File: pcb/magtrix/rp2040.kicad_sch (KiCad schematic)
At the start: 31 parts, among them J1 Conn_01x08_Pin, SW1 SW_MEC_5E, SW2 SW_MEC_5E, U1 W25Q128JVS, U3 RP2040, U4 AMS1117-3.3, Y1 12Mhz

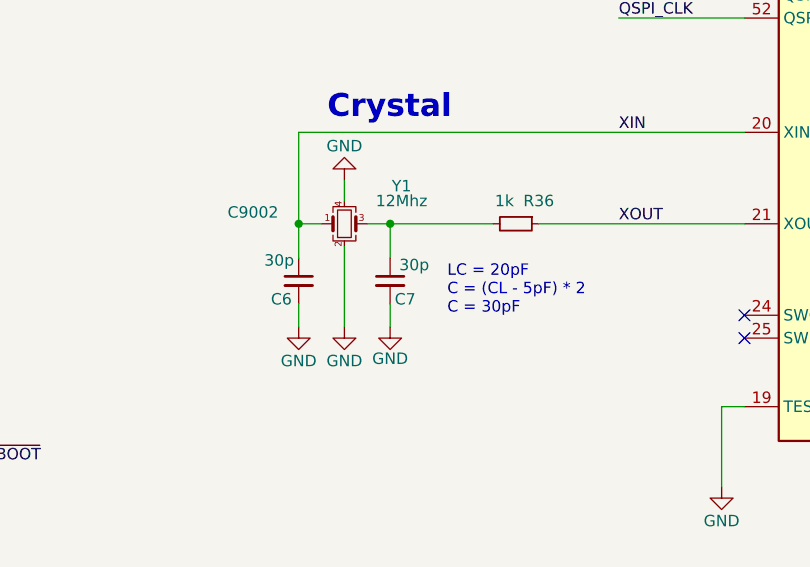
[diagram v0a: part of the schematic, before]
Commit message: Finished schematics and footprints, need to redo the placement
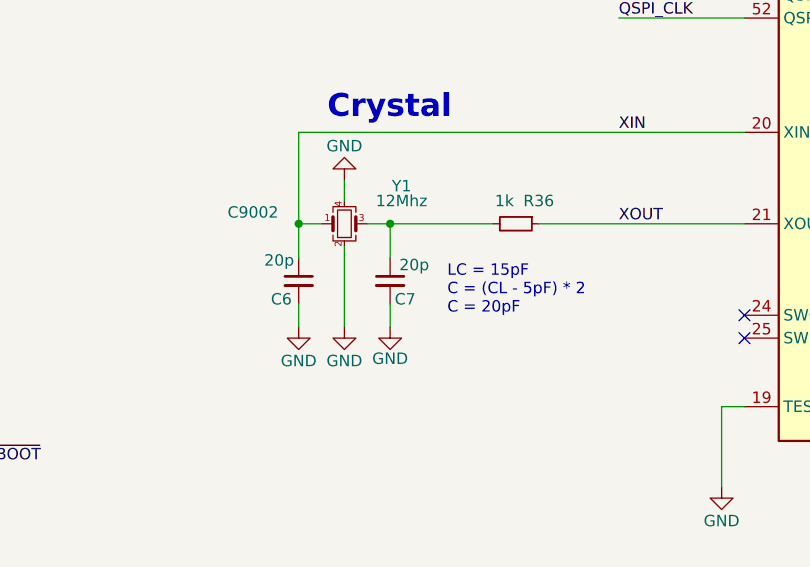
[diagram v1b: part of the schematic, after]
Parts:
- C10, C11: MFR (none) -> CL10A105KA8NNNC; MOUSER (none) -> 187-CL10A105KA8NNNC
- C12, C13, C14, C15, C16, C17, C3, C8, C9: MFR (none) -> TMK107BJ104KA-T; MOUSER (none) -> 963-TMK107BJ104KA-T
- C18, C19: footprint Capacitor_SMD:C_0603_1608Metric_Pad1.08x0.95mm_HandSolder -> Capacitor_SMD:C_1206_3216Metric; MFR (none) -> CL31A106MBHNNNE; MOUSER (none) -> 187-CL31A106MBHNNNE
- C6, C7: value 30p -> 20p; MFR (none) -> CL10C200JB8NNNC; MOUSER (none) -> 187-CL10C200JB8NNNC
- J1: footprint (none) -> Connector_PinHeader_1.00mm:PinHeader_1x08_P1.00mm_Vertical_SMD_Pin1Left
- R33, R35: MFR (none) -> CRCW060310K0JNEC; MOUSER (none) -> 71-CRCW060310K0JNEC
- R34, R36: footprint Resistor_SMD:R_0603_1608Metric -> Resistor_SMD:R_1206_3216Metric; MFR (none) -> ERJ-S08F1001V; MOUSER (none) -> 667-ERJ-S08F1001V
- R37, R38: MFR (none) -> CRCW060333R0JNEA; MOUSER (none) -> 71-CRCW0603J-33-E3
- R39, R40: MFR (none) -> CR0603AFX-5101EAS; MOUSER (none) -> 652-CR0603AFX5101EAS
- U1: MFR (none) -> W25Q128JVSIM; MOUSER (none) -> 454-W25Q128JVSIM
- U3: MFR (none) -> SC0914(13); MOUSER (none) -> 358-SC091413
- U4: MFR (none) -> LM1117MPX-3.3/NOPB; MOUSER (none) -> 926-LM1117MPX3.3NOPB
- Y1: footprint Crystal:Crystal_SMD_3225-4Pin_3.2x2.5mm -> CRYSTAL:crystal; MFR (none) -> 830069944; MOUSER (none) -> 710-830069944
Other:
- note added: "LC = 15pF C = (CL - 5pF) * 2 C = 20pF"
- note removed: "LC = 20pF C = (CL - 5pF) * 2 C = 30pF"

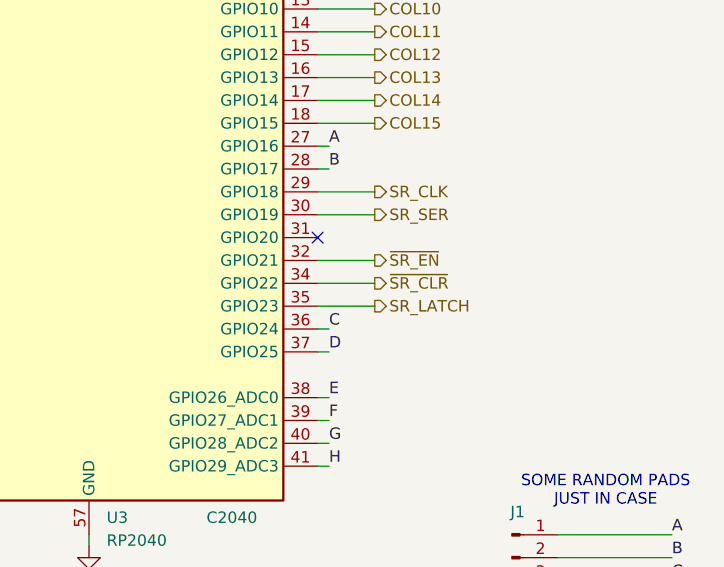
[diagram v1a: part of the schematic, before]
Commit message: Changed shift registers to open drain ones
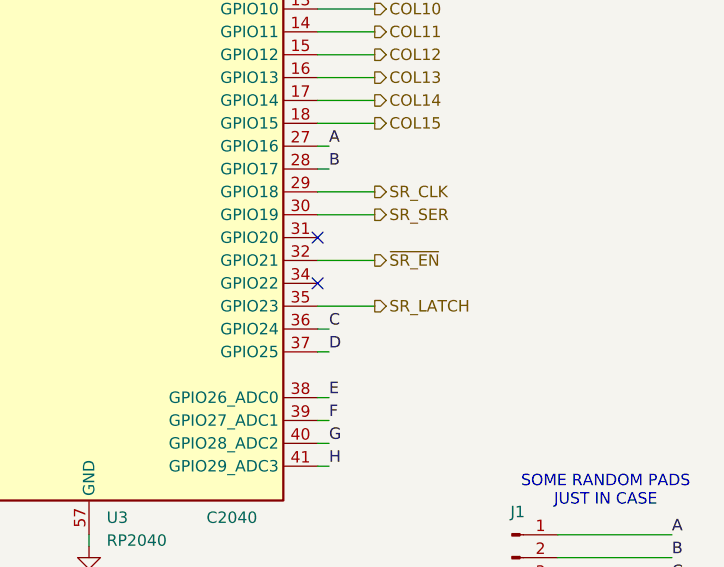
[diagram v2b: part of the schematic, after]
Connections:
- net ~{SR_CLR}: no longer names the net of U3.34 (GPIO22)
- no-connect marks 5 -> 6
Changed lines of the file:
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@@
+	)
+	(no_connect
+		(at 233.68 116.84)
 	)
 	(no_connect
@@
 		(pts
 			(xy 182.88 137.16) (xy 180.34 137.16)
-		)
-		(stroke
-			(width 0)
-			(type default)
-		)
-	)
-	(wire
-		(pts
-			(xy 233.68 116.84) (xy 240.03 116.84)
 		)
 		(stroke
@@
 		(fields_autoplaced yes)
 		(effects
-			(font
-				(size 1.27 1.27)
-			)
-			(justify left)
-		)
-	)
-	(hierarchical_label "~{SR_CLR}"
-		(shape output)
-		(at 240.03 116.84 0)
-		(fields_autoplaced yes)
-		(effects

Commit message: Added finished PCB
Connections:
- net COL13: no longer names the net of U3.16 (GPIO13)
- net COL14: no longer names the net of U3.17 (GPIO14)
- net COL15: no longer names the net of U3.18 (GPIO15)
- no-connect marks 6 -> 9
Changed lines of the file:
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@@
+	)
+	(no_connect
+		(at 233.68 96.52)
 	)
 	(no_connect
@@
 	)
 	(no_connect
+		(at 233.68 99.06)
+	)
+	(no_connect
 		(at 233.68 116.84)
 	)
@@
 		(at 59.69 49.53)
 	)
+	(no_connect
+		(at 233.68 93.98)
+	)
 	(wire
 		(pts
@@
 	(wire
 		(pts
-			(xy 233.68 96.52) (xy 240.03 96.52)
-		)
-		(stroke
-			(width 0)
-			(type default)
-		)
-	)
-	(wire
-		(pts
 			(xy 137.16 74.93) (xy 137.16 73.66)
 		)
@@
 	(wire
 		(pts
-			(xy 233.68 93.98) (xy 240.03 93.98)
-		)
-		(stroke
-			(width 0)
-			(type default)
-		)
-	)
-	(wire
-		(pts
 			(xy 80.645 47.625) (xy 80.645 48.895)
 		)
@@
 		(pts
 			(xy 261.62 37.465) (xy 261.62 39.37)
-		)
-		(stroke
-			(width 0)
-			(type default)
-		)
-	)
-	(wire
-		(pts
-			(xy 233.68 99.06) (xy 240.03 99.06)
 		)
 		(stroke
@@
 		)
 	)
-	(hierarchical_label "COL14"
-		(shape output)
-		(at 240.03 96.52 0)
-		(fields_autoplaced yes)
-		(effects
-			(font
-				(size 1.27 1.27)
-			)
-			(justify left)
-		)
-	)
 	(hierarchical_label "COL11"
 		(shape output)
@@
 		)
 	)
-	(hierarchical_label "COL13"
-		(shape output)
-		(at 240.03 93.98 0)
-		(fields_autoplaced yes)
-		(effects
-			(font
-				(size 1.27 1.27)
-			)
-			(justify left)
-		)
-	)
 	(hierarchical_label "COL4"
 		(shape output)
@@
 		(fields_autoplaced yes)
 		(effects
-			(font
-				(size 1.27 1.27)
-			)
-			(justify left)
-		)
-	)
-	(hierarchical_label "COL15"
-		(shape output)
-		(at 240.03 99.06 0)
-		(fields_autoplaced yes)
-		(effects
